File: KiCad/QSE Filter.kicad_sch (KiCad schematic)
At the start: 64 parts, among them J1 RF In, J2 RF Out, J3 Power, J4 Control In, Q1 2N7002, Q2 2N7002, Q4 2N7002, Q5 2N7002, U1 EB2-12NU, U2 EB2-12NU, U4 EB2-12NU, U5 EB2-12NU

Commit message: Created project symbol and footprint libraries
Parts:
- C1, C10, C2, C23, C24, C3, C30, C31, C9: symbol Device:C_Small -> QSE Filter:C_Small
- C11, C12, C13, C14, C15, C16, C17, C18, C19, C20, C25, C26, C27, C28, C29, C32, C33, C34, C35, C36, C4, C5, C6, C7, C8: symbol Device:C -> QSE Filter:C
- D1, D2, D4, D5: symbol Diode:1N4148WS -> QSE Filter:1N4148WS
- J1, J2: symbol Connector:Conn_Coaxial -> QSE Filter:Conn_Coaxial
- J3: symbol Connector_Generic:Conn_02x08_Odd_Even -> QSE Filter:Conn_02x08_Odd_Even
- J4: symbol Connector_Generic:Conn_02x05_Odd_Even -> QSE Filter:Conn_02x05_Odd_Even
- L1, L10, L2, L3, L4, L5, L6, L7, L8, L9: symbol Device:L -> QSE Filter:L
- Q1, Q2, Q4, Q5: symbol Transistor_FET:2N7002 -> QSE Filter:2N7002
- R1, R2, R3, R4: symbol Device:R -> QSE Filter:R
- U1, U2, U4, U5: symbol Kemet EB2-12NU-L:EB2-12NU -> QSE Filter:EB2-12NU

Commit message: Corrected RF connector symbol so KiCad will stop disconnecting pins 3, 4, 5, by creating a stack of invisible pins Updated all footprints and symbols to pull from the QSE Filter library
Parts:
- C1, C10, C11, C12, C13, C14, C15, C16, C17, C18, C19, C2, C20, C23, C24, C25, C26, C27, C28, C29, C3, C30, C31, C32, C33, C34, C35, C36, C4, C5, C6, C7, C8, C9: footprint Capacitor_SMD:C_0805_2012Metric -> QSE Filter:C_0805_2012Metric
- D1, D2, D4, D5: footprint Diode_SMD:D_SOD-323 -> QSE Filter:D_SOD-323
- J1, J2: footprint DigiKey:CONN_RF2-04A-T-00-50-G_ADM -> QSE Filter:CONN_RF2-04A-T-00-50-G_ADM
- J3: footprint Connector_IDC:IDC-Header_2x08_P2.54mm_Vertical -> QSE Filter:IDC-Header_2x08_P2.54mm_Vertical
- J4: footprint Connector_IDC:IDC-Header_2x05_P2.54mm_Vertical -> QSE Filter:IDC-Header_2x05_P2.54mm_Vertical
- L1, L10, L2, L3, L4, L5, L7, L8, L9: footprint DigiKey:IND_1008CS_COC -> QSE Filter:IND_1008CS_COC
- L6: footprint DigiKey:INDC2015X152N -> QSE Filter:INDC2015X152N
- Q1, Q2, Q4, Q5: footprint Package_TO_SOT_SMD:SOT-23 -> QSE Filter:SOT-23
- R1, R2, R3, R4: footprint Resistor_SMD:R_0805_2012Metric -> QSE Filter:R_0805_2012Metric
- U1, U2, U4, U5: footprint DigiKey:EB2-12NU_KEM -> QSE Filter:EB2-12NU_KEM
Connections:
- net GND: now also J1.3 (Ext), J1.4 (Ext), J1.5 (Ext), J2.3 (Ext), J2.4 (Ext), J2.5 (Ext)

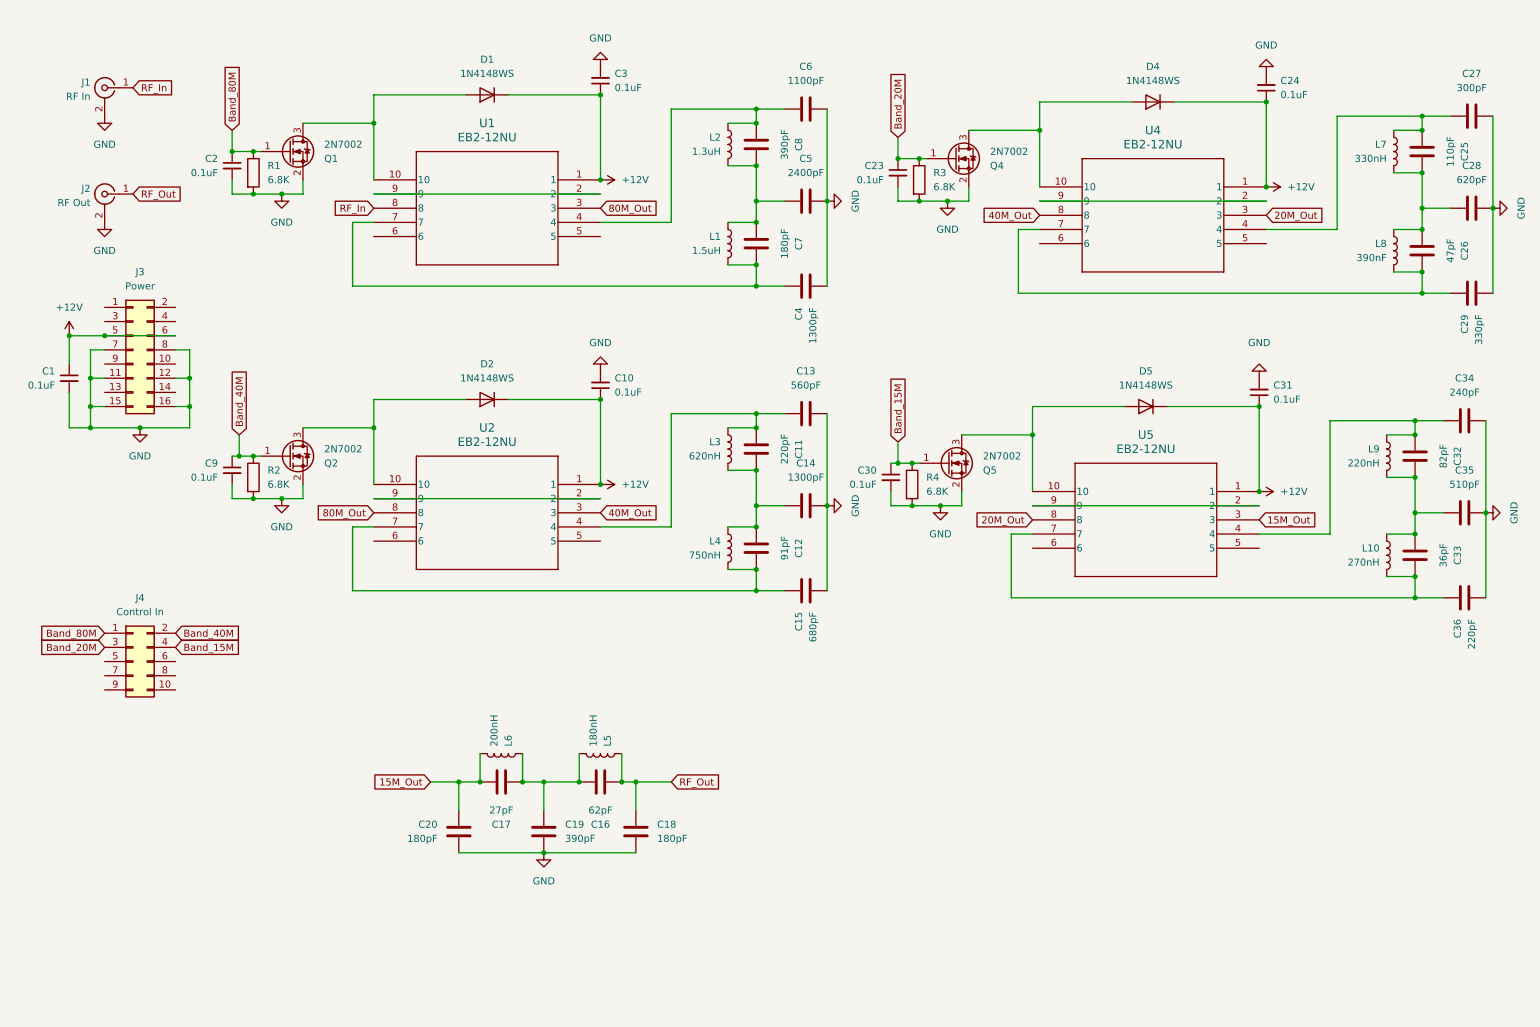
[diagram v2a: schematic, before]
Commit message: Added switched 10m LPF using a 4-input NOR gate to control the 10m filter relay
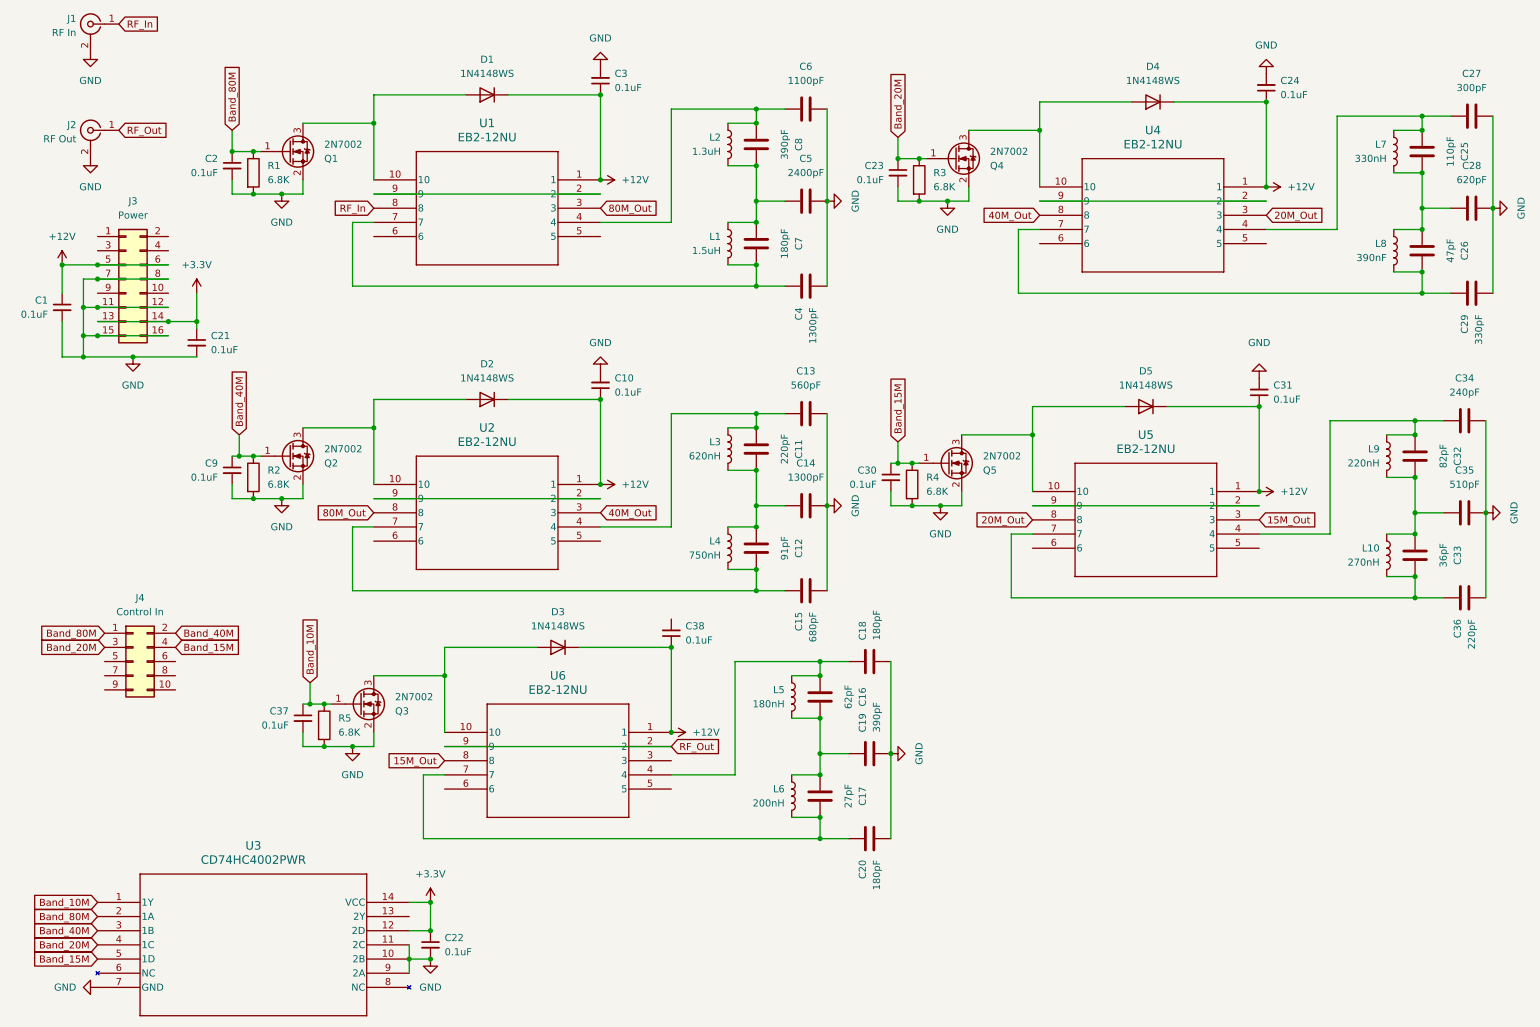
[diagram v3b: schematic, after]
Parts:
- added C21, C22: 0.1uF, symbol Device:C_Small
- added C37, C38: 0.1uF, QSE Filter:C_0805_2012Metric, symbol QSE Filter:C_Small
- added D3: 1N4148WS, QSE Filter:D_SOD-323, symbol QSE Filter:1N4148WS
- added Q3: 2N7002, QSE Filter:SOT-23, symbol QSE Filter:2N7002
- added R5: 6.8K, QSE Filter:R_0805_2012Metric, symbol QSE Filter:R
- added U3: CD74HC4002PWR, PW14, symbol QSE Filter:CD74HC4002PWR
- added U6: EB2-12NU, QSE Filter:EB2-12NU_KEM, symbol QSE Filter:EB2-12NU
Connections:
- net +12V: now also C38.1, D3.1 (K), U6.1
- net 15M_Out: now also U6.8; no longer C17.1, C20.1, L6.1
- net Band_15M: now also U3.5 (1D)
- net Band_20M: now also U3.4 (1C)
- net Band_40M: now also U3.3 (1B)
- net Band_80M: now also U3.2 (1A)
- net GND: now also C21.2, C22.2, C37.2, Q3.2 (S), R5.2, U3.10 (2B), U3.11 (2C), U3.7 (GND), U3.9 (2A)
- net RF_Out: now also U6.2, U6.9; no longer C16.2, C18.1, L5.2
- net +3.3V: now reaches J3.13 (Pin_13)
- net +3.3V: now also J3.14 (Pin_14), C21.1, C22.1, U3.12 (2D), U3.14 (VCC)
- new net: C17.1, C20.1, L6.1, U6.7
- new net: C16.2, C18.1, L5.2, U6.4
- new net: D3.2 (A), Q3.3 (D), U6.10
- new net Band_10M: C37.1, Q3.1 (G), R5.1, U3.1 (1Y)
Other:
- moved on the sheet: C1, C16, C17, C18, C19, C20, J1, J2, J3, L5, L6

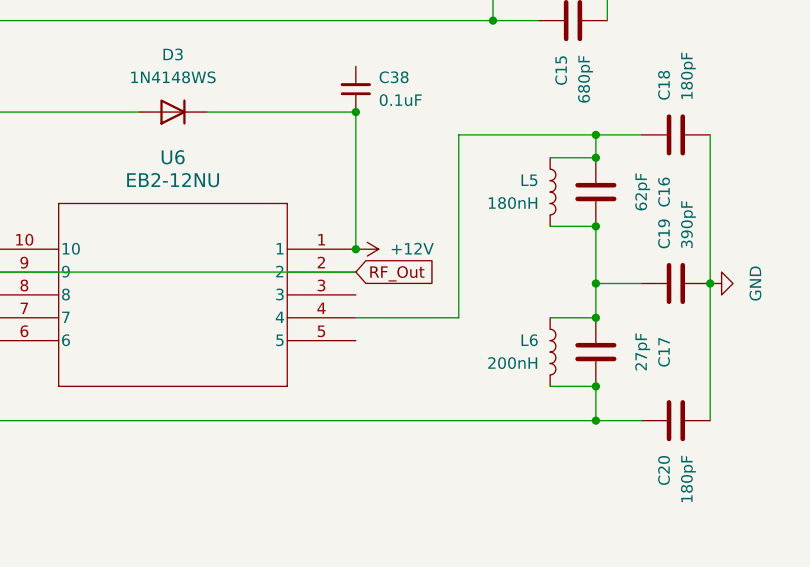
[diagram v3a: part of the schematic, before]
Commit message: Assigned C21 and C22 footprints Corrected RF out pin on U6
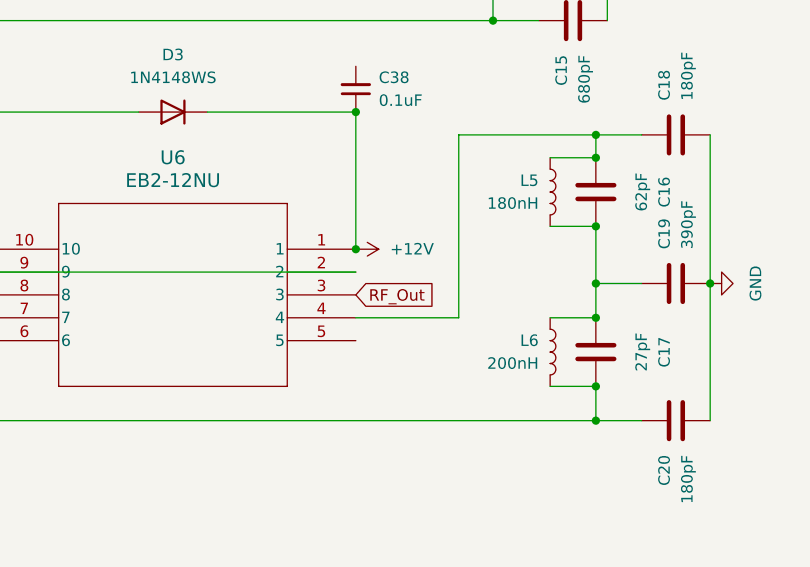
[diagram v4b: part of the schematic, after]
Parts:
- C21, C22: footprint (none) -> QSE Filter:C_0805_2012Metric
- U3: footprint PW14 -> QSE Filter:PW14
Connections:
- net RF_Out: now also U6.3; no longer U6.2, U6.9
- new net: U6.2, U6.9
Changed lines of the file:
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@@
+    )
+  )
+  (global_label "RF_Out" (shape input) (at 130.81 149.86 0) (fields_autoplaced)
+    (effects (font (size 1.27 1.27)) (justify left))
+    (property "Intersheetrefs" "${INTERSHEET_REFS}" (at 140.3266 149.86 0)
+      (effects (font (size 1.27 1.27)) (justify left) hide)
     )
   )
@@
     )
   )
-  (global_label "RF_Out" (shape input) (at 130.81 147.32 0) (fields_autoplaced)
-    (effects (font (size 1.27 1.27)) (justify left))
-    (property "Intersheetrefs" "${INTERSHEET_REFS}" (at 140.3266 147.32 0)
-      (effects (font (size 1.27 1.27)) (justify left) hide)
-    )
-  )
   (global_label "Band_40M" (shape input) (at 27.94 180.34 180) (fields_autoplaced)
     (effects (font (size 1.27 1.27)) (justify right))
@@
       (effects (font (size 1.524 1.524)))
     )
-    (property "Footprint" "PW14" (at 27.94 175.26 0)
+    (property "Footprint" "QSE Filter:PW14" (at 27.94 175.26 0)
       (effects (font (size 1.27 1.27) italic) hide)
     )
@@
       (effects (font (size 1.27 1.27)) (justify left))
     )
-    (property "Footprint" "" (at 87.63 182.88 0)
+    (property "Footprint" "QSE Filter:C_0805_2012Metric" (at 87.63 182.88 0)
       (effects (font (size 1.27 1.27)) hide)
     )
@@
       (effects (font (size 1.27 1.27)) (justify left))
     )
-    (property "Footprint" "" (at 45.72 74.93 0)
-      (effects (font (size 1.27 1.27)) hide)
-    )
+    (property "Footprint" "QSE Filter:C_0805_2012Metric" (at 45.72 74.93 0)
+      (effects (font (size 1.27 1.27)) hide)
+    )

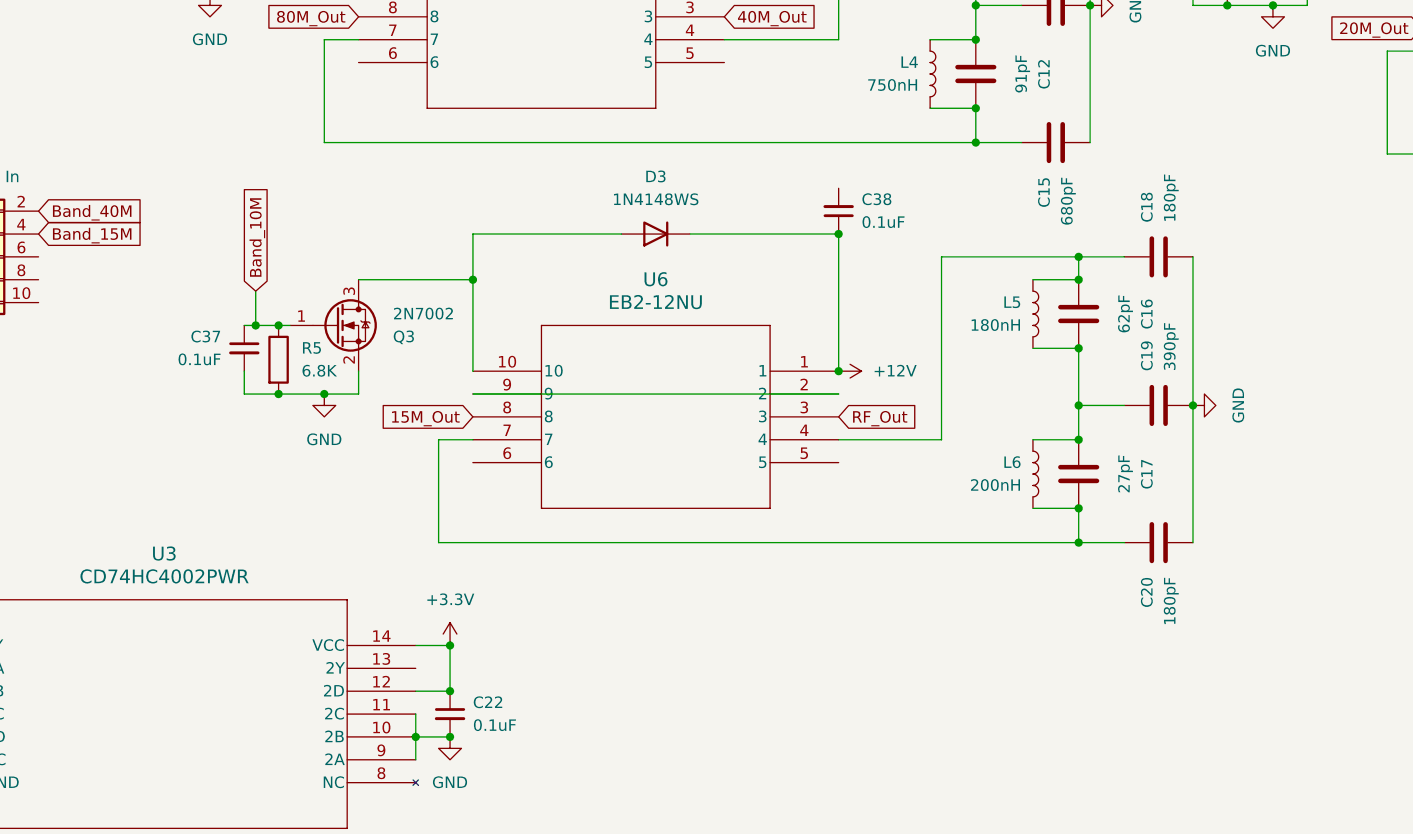
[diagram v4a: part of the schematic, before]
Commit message: Ground C38 pin 2
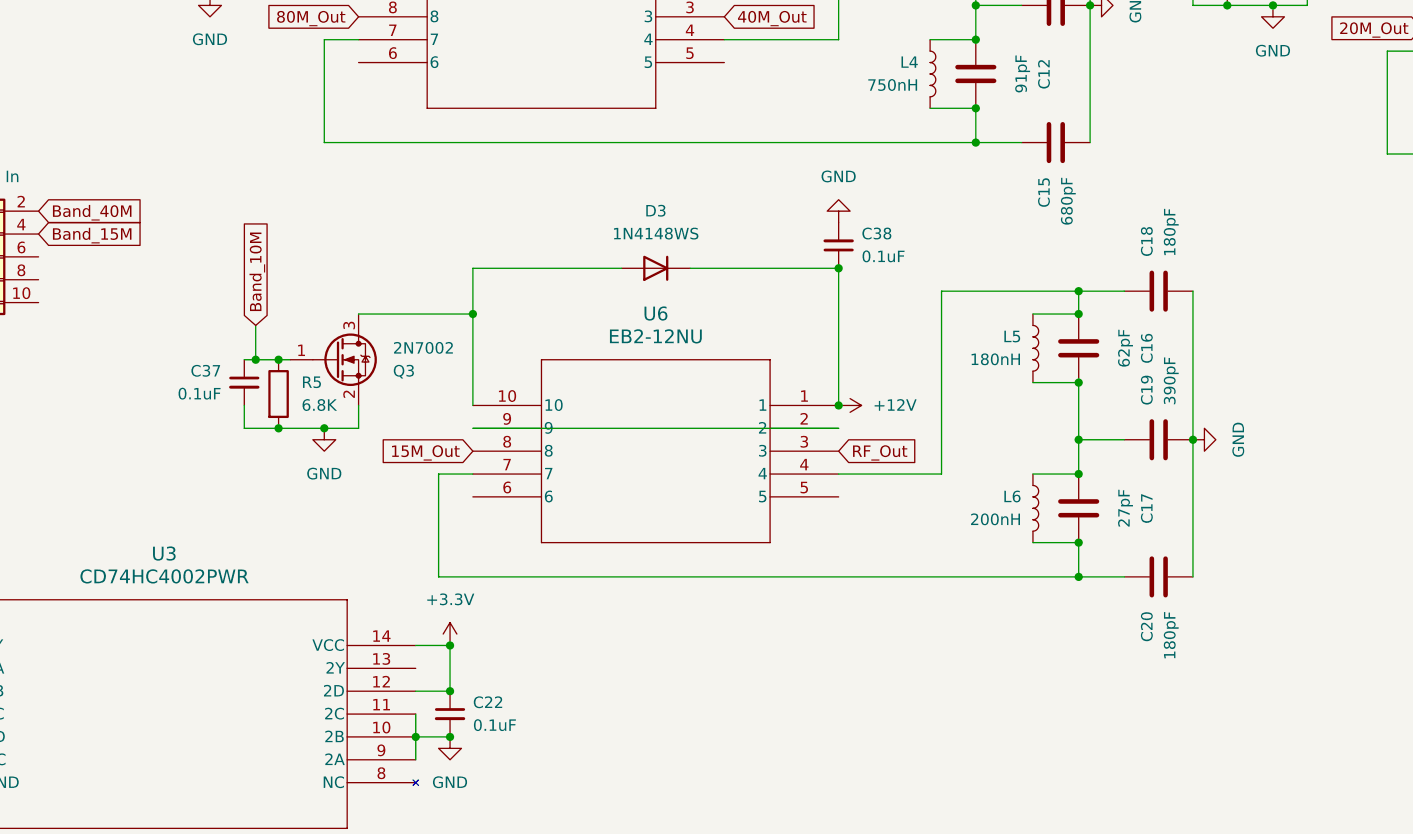
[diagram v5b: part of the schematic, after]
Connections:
- net GND: now also C38.2
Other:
- moved on the sheet: C16, C17, C18, C19, C20, C37, C38, D3, L5, L6, Q3, R5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
